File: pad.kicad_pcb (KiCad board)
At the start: 2 copper layers, 142.7 x 72.9 mm, 51 parts, among them U1 LPV324MX, U2 ULN2002, U3 LM339

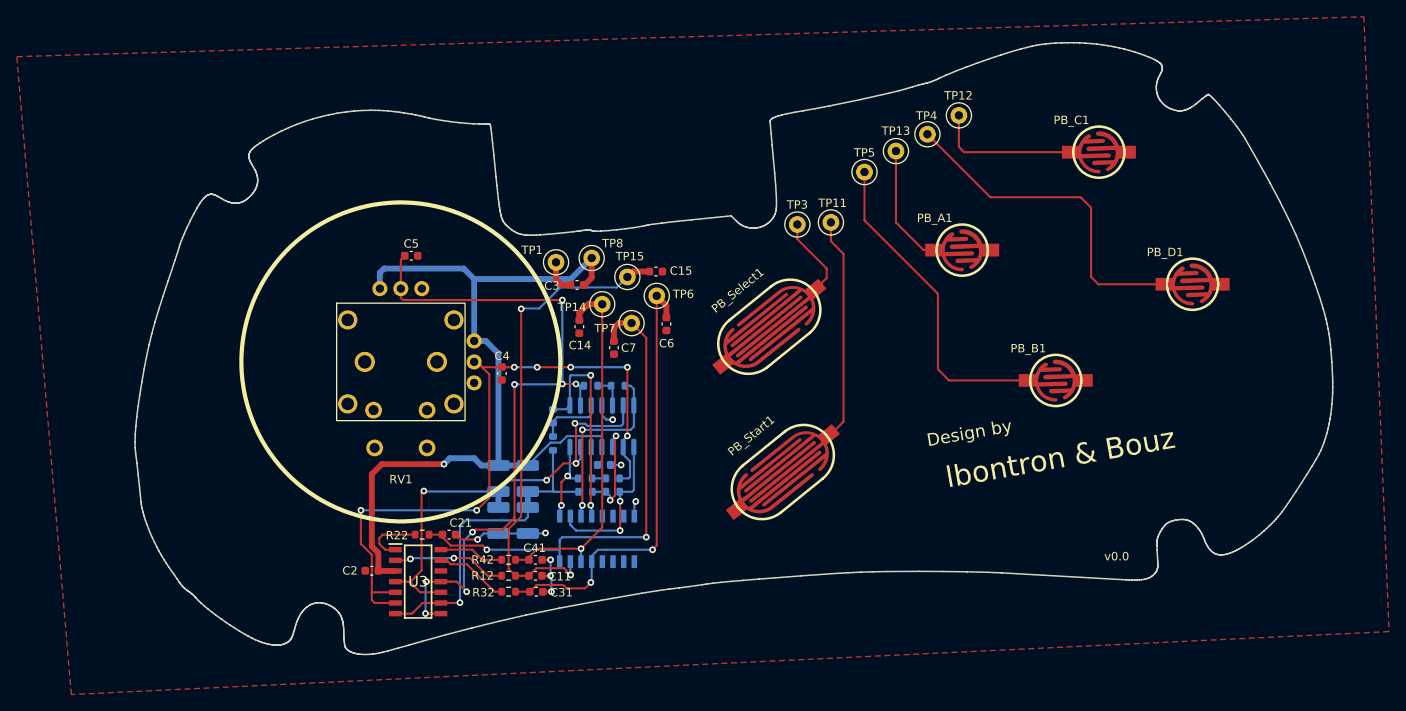
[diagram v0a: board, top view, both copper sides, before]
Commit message: Update board size
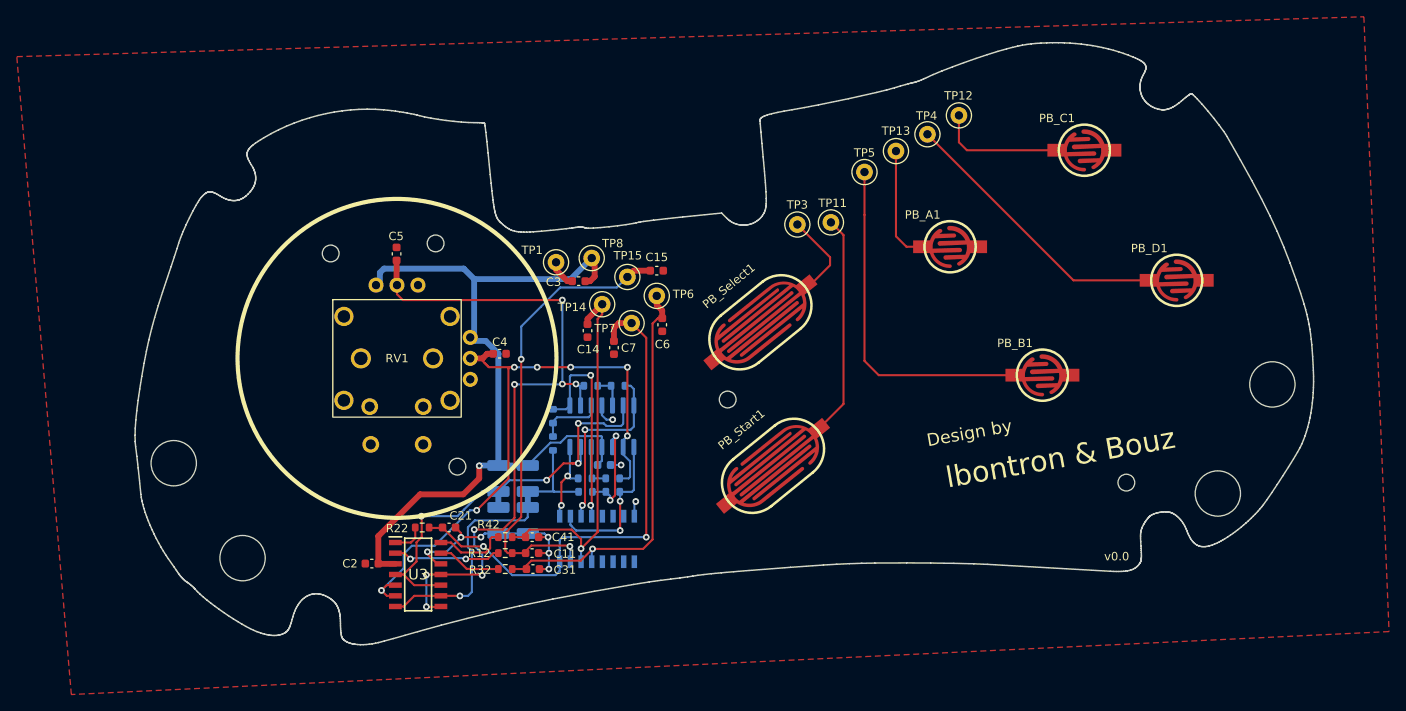
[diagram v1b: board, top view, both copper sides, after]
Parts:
- moved C31 2.73 mm to (97.5, 112.8)
- moved C41 2.73 mm to (97.4, 109.0)
- moved R32 2.73 mm to (94.2, 112.8)
- moved R42 2.73 mm to (94.2, 109.0)
- moved C11 2.73 mm to (97.4, 110.9)
- moved R12 2.73 mm to (94.2, 110.9)
- moved C4 2.37 mm to (93.5, 87.2), turned to 0 degrees
- moved PB_D1 1.95 mm to (174.2, 78.4)
- moved C5 1.76 mm to (81.2, 75.2), turned to 90 degrees
- moved PB_C1 1.75 mm to (163.2, 62.9)
- moved PB_B1 1.71 mm to (158.2, 89.7)
- moved PB_A1 1.49 mm to (147.2, 74.4)
- moved PB_Start1 1.38 mm to (126.1, 100.5)
- moved PB_Select1 1.19 mm to (124.6, 83.4)
- moved C14 1.08 mm to (104.0, 84.4)
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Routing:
- net GND: track 27.9 -> 35.6 mm, vias 8 -> 9
- net xAxis: track 83.0 -> 75.4 mm
- net Net-(PB_D1-Pad2): track 40.6 -> 33.6 mm
- net +5V: track 104.3 -> 98.2 mm
- net TP6_RIG: track 54.0 -> 50.1 mm, vias 2 -> 1
- net Net-(R22-Pad1): track 7.33 -> 3.86 mm
- net TP7_BOT: track 59.7 -> 62.7 mm
- net TP15_TOP: track 58.8 -> 56.0 mm
- net Net-(PB_B1-Pad2): track 38.5 -> 41.1 mm
- net VRef_p: track 54.1 -> 51.9 mm
- net Net-(PB_C1-Pad2): track 17.4 -> 15.3 mm
- net Net-(R32-Pad1): track 8.79 -> 7.63 mm
- net yAxis: track 85.8 -> 84.7 mm
- net TP14_LEF: track 44.3 -> 45.3 mm
- net Net-(R42-Pad1): track 7.74 -> 8.75 mm
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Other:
- board size 142.7 x 72.9 mm -> 140.4 x 71.7 mm
